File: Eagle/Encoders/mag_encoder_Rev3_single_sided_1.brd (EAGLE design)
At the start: 12.9 x 24 mm, 5 parts, among them IC1 A1203LH

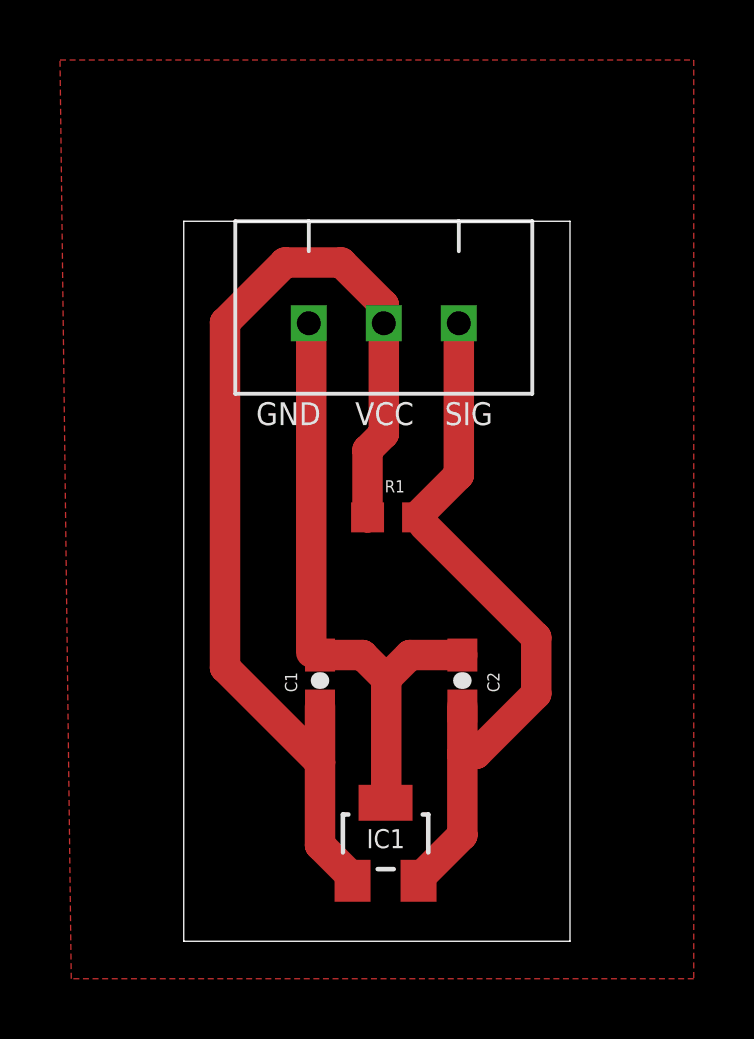
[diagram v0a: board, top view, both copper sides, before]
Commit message: Made changes to single-sided encoder boards and updated gcode that works for Lawlor's CNC router.
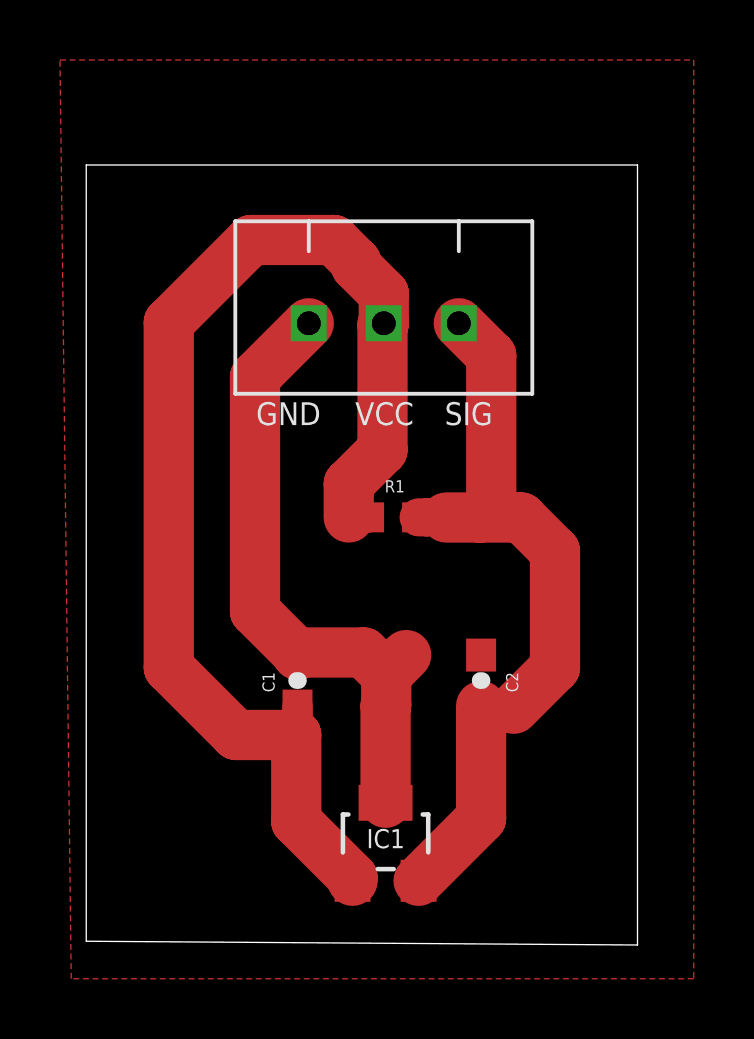
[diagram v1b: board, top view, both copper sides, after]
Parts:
- moved C1 0.75 mm to (6.92, 10.2)
- moved C2 0.62 mm to (13.0, 10.2)
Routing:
- net VCC: track 36.7 -> 41.0 mm
- net SIG: track 24.4 -> 26.0 mm
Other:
- board size 12.9 x 24 mm -> 18.4 x 26 mm
